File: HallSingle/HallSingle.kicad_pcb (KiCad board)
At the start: 2 copper layers, 12 x 23.5 mm, 12 parts, among them J1 Conn_01x03, U1 SS49E, U2 TS331ILT

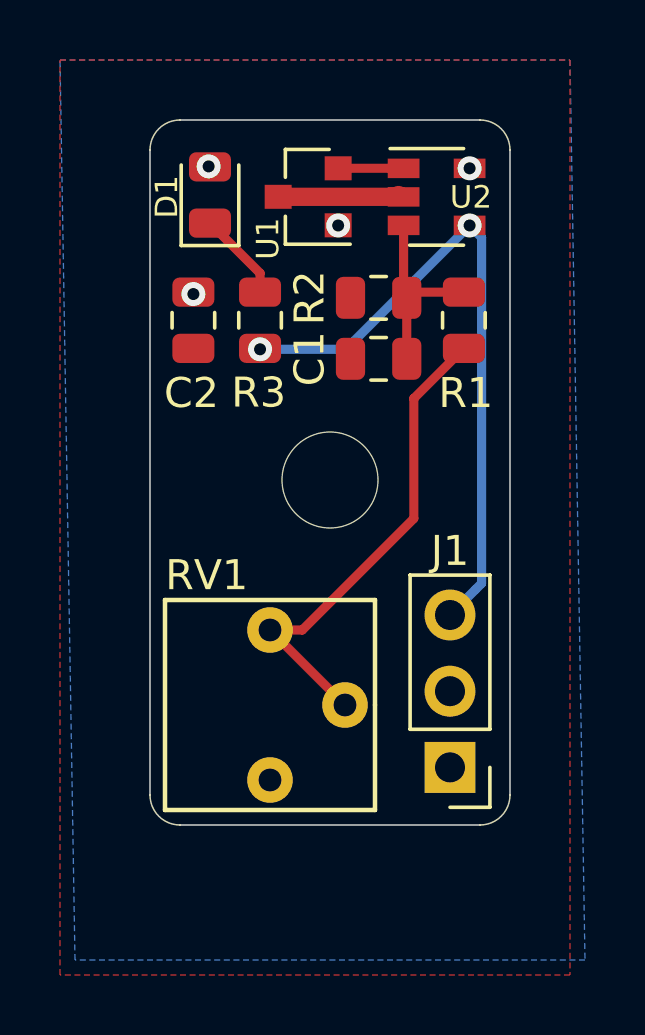
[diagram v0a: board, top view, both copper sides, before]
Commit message: Changed comparator to reverse - also NOTed  the led. this is to help with fault tolerance
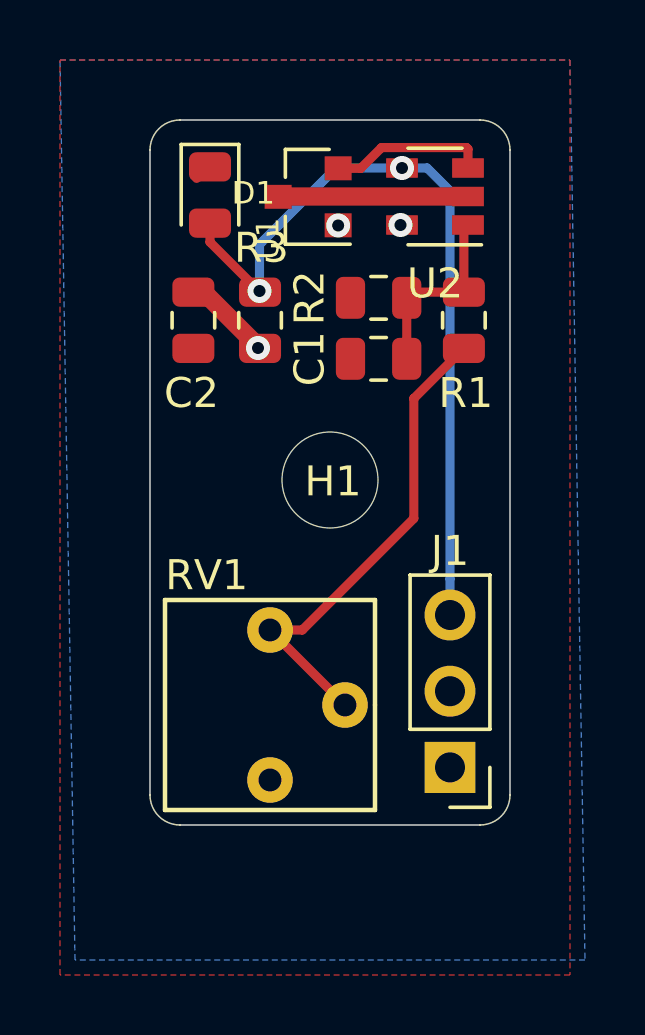
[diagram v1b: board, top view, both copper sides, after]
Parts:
- removed G***: LOGO, HallEffect:VoronLogo_6pt5mm_silkScreen
- removed REF**: MountingHole_3.2mm_M3, HallEffect:MountingHole_3.2mm_M3
- added H1: MountingHole, HallEffect:MountingHole_3.2mm_M3, F.Cu at (144.0, 69.0)
- U2: value TS331ILT -> TL331; footprint HallEffect:SOT-23-5 -> Package_TO_SOT_SMD:SOT-23-5
- moved U2 0.06 mm to (147.5, 59.5), turned to 180 degrees
- turned D1 to 270 degrees
- turned R3 to 90 degrees
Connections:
- D1 pad 1: Net-(D1-Pad1) -> GND
- D1 pad 2: +5V -> Signal
- R3 pad 1: Net-(D1-Pad1) -> +5V
- U2 pad 1: Net-(U1-Pad2) -> Net-(C1-Pad1)
- U2 pad 3: Net-(C1-Pad1) -> Net-(U1-Pad2)
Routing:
- net Signal: track 22.3 -> 26.5 mm
- net Net-(U1-Pad2): track 2.18 -> 5.27 mm
- net +5V: track 0.00 -> 3.00 mm, vias 4 -> 3
- net Net-(D1-Pad1): track 2.99 -> 0.00 mm
- net GND: track 4.27 -> 6.90 mm

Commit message: Resolved some design rule issues. update jpg
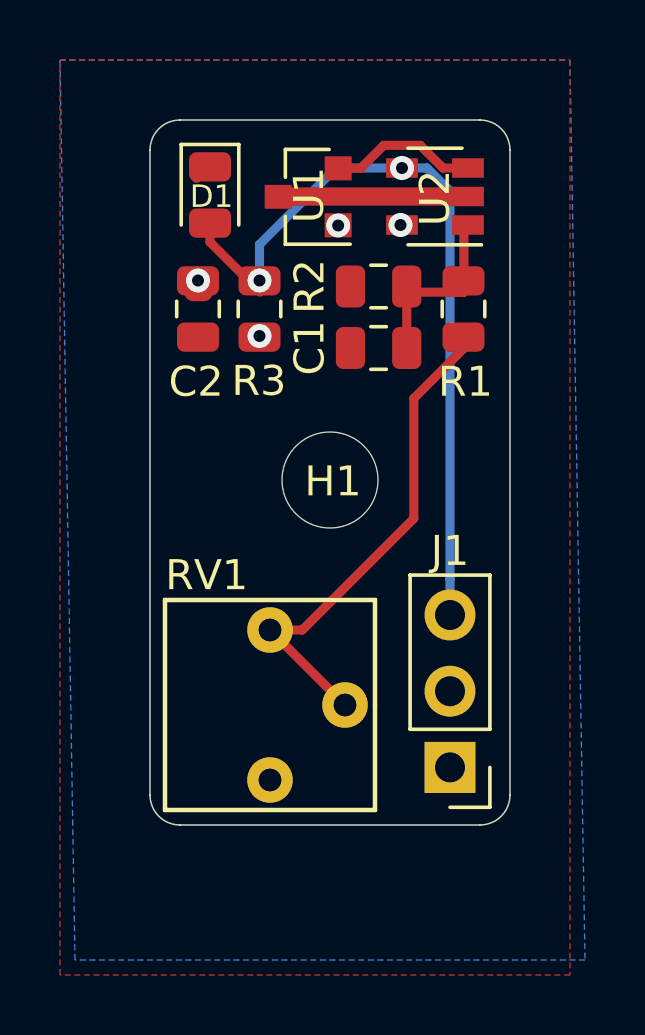
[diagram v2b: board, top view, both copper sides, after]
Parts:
- moved C2 0.41 mm to (139.6, 63.3)
- moved R2 0.38 mm to (145.6, 62.5)
- moved R3 0.38 mm to (141.7, 63.3)
- moved R1 0.38 mm to (148.4, 63.3)
- moved C1 0.36 mm to (145.6, 64.6)
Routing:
- net +5V: track 3.00 -> 0.35 mm, vias 3 -> 4
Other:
- board text added: "NC V1.0"

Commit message: Corrected wiring to comparator to NC config. Updated header to be same config as SKR - straight through cable required. update revision number
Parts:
- turned U2 to 0 degrees
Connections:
- J1 pad 1: +5V -> Signal
- J1 pad 3: Signal -> +5V
- U2 pad 1: Net-(C1-Pad1) -> Net-(U1-Pad2)
- U2 pad 3: Net-(U1-Pad2) -> Net-(C1-Pad1)
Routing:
- net +5V: track 0.35 -> 4.45 mm
- net Signal: track 26.5 -> 30.5 mm
- net Net-(U1-Pad2): track 4.96 -> 2.14 mm
- net GND: track 6.90 -> 4.70 mm
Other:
- board text added: "NC V1.1"
- board text removed: "NC V1.0"
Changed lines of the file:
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@@
     (thickness 1.6)
     (drawings 12)
-    (tracks 40)
+    (tracks 51)
     (zones 0)
     (modules 11)
@@
   )
   (module Package_TO_SOT_SMD:SOT-23-5 (layer F.Cu)
-    (at 147.5 59.55 180)
+    (at 147.5 59.55)
     (descr "5-pin SOT23 package")
     (tags SOT-23-5)
@@
       (effects (font (size 0.5 0.5) (thickness 0.075)))
     )
-    (pad 5 smd rect (at 1.1 -0.95 180) (size 1.06 0.65) (layers F.Cu F.Paste F.Mask)
+    (pad 5 smd rect (at 1.1 -0.95) (size 1.06 0.65) (layers F.Cu F.Paste F.Mask)
       (net 3 +5V))
-    (pad 4 smd rect (at 1.1 0.95 180) (size 1.06 0.65) (layers F.Cu F.Paste F.Mask)
+    (pad 4 smd rect (at 1.1 0.95) (size 1.06 0.65) (layers F.Cu F.Paste F.Mask)
       (net 4 Signal))
-    (pad 3 smd rect (at -1.1 0.95 180) (size 1.06 0.65) (layers F.Cu F.Paste F.Mask)
+    (pad 3 smd rect (at -1.1 0.95) (size 1.06 0.65) (layers F.Cu F.Paste F.Mask)
+      (net 2 "Net-(C1-Pad1)"))
+    (pad 2 smd rect (at -1.1 0) (size 1.06 0.65) (layers F.Cu F.Paste F.Mask)
+      (net 1 GND))
+    (pad 1 smd rect (at -1.1 -0.95) (size 1.06 0.65) (layers F.Cu F.Paste F.Mask)
       (net 6 "Net-(U1-Pad2)"))
-    (pad 2 smd rect (at -1.1 0 180) (size 1.06 0.65) (layers F.Cu F.Paste F.Mask)
-      (net 1 GND))
-    (pad 1 smd rect (at -1.1 -0.95 180) (size 1.06 0.65) (layers F.Cu F.Paste F.Mask)
-      (net 2 "Net-(C1-Pad1)"))
     (model ${KISYS3DMOD}/Package_TO_SOT_SMD.3dshapes/SOT-23-5.wrl
       (at (xyz 0 0 0))
@@
     (fp_line (start -0.635 -1.27) (end 1.27 -1.27) (layer F.Fab) (width 0.1))
     (pad 3 thru_hole oval (at 0 5.08 180) (size 1.7 1.7) (drill 1) (layers *.Cu *.Mask)
+      (net 3 +5V))
+    (pad 2 thru_hole oval (at 0 2.54 180) (size 1.7 1.7) (drill 1) (layers *.Cu *.Mask)
+      (net 1 GND))
+    (pad 1 thru_hole rect (at 0 0 180) (size 1.7 1.7) (drill 1) (layers *.Cu *.Mask)
       (net 4 Signal))
-    (pad 2 thru_hole oval (at 0 2.54 180) (size 1.7 1.7) (drill 1) (layers *.Cu *.Mask)
-      (net 1 GND))
-    (pad 1 thru_hole rect (at 0 0 180) (size 1.7 1.7) (drill 1) (layers *.Cu *.Mask)
-      (net 3 +5V))
     (model ${KIPRJMOD}/Library/3D_Packages/PinHeader_1x03_P2.54mm_Vertical.step
       (at (xyz 0 0 0))
@@
     )
   )
-  (gr_text "NC V1.0\n" (at 139.15 69.05 90) (layer B.SilkS)
+  (gr_text "NC V1.1\n" (at 139.15 69.05 90) (layer B.SilkS)
     (effects (font (size 1 1) (thickness 0.15)) (justify mirror))
   )
@@
   (gr_line (start 150 58) (end 150 79.5) (layer Edge.Cuts) (width 0.05))
   (gr_line (start 139 57) (end 149 57) (layer Edge.Cuts) (width 0.05))
+  (segment (start 139.554001 58.946999) (end 139.954 58.547) (width 0.3048) (layer F.Cu) (net 1))
   (segment (start 142.2825 59.55) (end 142.272 59.5605) (width 0.6096) (layer F.Cu) (net 1))
-  (segment (start 148.6 59.55) (end 142.2825 59.55) (width 0.6096) (layer F.Cu) (net 1))
-  (segment (start 139.554001 58.946999) (end 139.954 58.547) (width 0.3048) (layer F.Cu) (net 1))
+  (segment (start 146.4 59.55) (end 142.2825 59.55) (width 0.6096) (layer F.Cu) (net 1))
   (segment (start 148.45 62.725) (end 148.463 62.738) (width 0.3048) (layer F.Cu) (net 2))
   (segment (start 147.9885 62.738) (end 148.463 62.738) (width 0.3048) (layer F.Cu) (net 2))
   (segment (start 146.4535 62.824) (end 146.558 62.9285) (width 0.3048) (layer F.Cu) (net 2))
   (segment (start 146.7485 62.738) (end 146.558 62.9285) (width 0.3048) (layer F.Cu) (net 2))
-  (segment (start 148.463 62.738) (end 146.7485 62.738) (width 0.3048) (layer F.Cu) (net 2))
+  (segment (start 148.463 62.45) (end 146.7485 62.45) (width 0.3048) (layer F.Cu) (net 2))
   (segment (start 146.558 64.9605) (end 146.558 62.9285) (width 0.3048) (layer F.Cu) (net 2))
-  (segment (start 148.463 60.637) (end 148.6 60.5) (width 0.3048) (layer F.Cu) (net 2))
-  (segment (start 148.463 62.738) (end 148.463 60.637) (width 0.3048) (layer F.Cu) (net 2))
-  (via (at 141.65 64.2) (size 0.8) (drill 0.4) (layers F.Cu B.Cu) (net 3))
-  (via (at 146.35 60.5) (size 0.8) (drill 0.4) (layers F.Cu B.Cu) (net 3))
-  (via (at 144.272 60.5155) (size 0.8) (drill 0.4) (layers F.Cu B.Cu) (net 3))
+  (segment (start 146.4 62.392) (end 146.558 62.55) (width 0.3048) (layer F.Cu) (net 2))
+  (segment (start 146.4 60.5) (end 146.4 62.392) (width 0.3048) (layer F.Cu) (net 2))
+  (via (at 142.4 63.5) (size 0.8) (drill 0.4) (layers F.Cu B.Cu) (net 3))
+  (via (at 145.15 60.5) (size 0.8) (drill 0.4) (layers F.Cu B.Cu) (net 3))
   (segment (start 139.446 62.738) (end 139.446 62.738) (width 0.6096) (layer F.Cu) (net 3))
   (segment (start 139.446 62.738) (end 139.7935 62.738) (width 0.6096) (layer F.Cu) (net 3))
-  (via (at 139.6 62.35) (size 0.8) (drill 0.4) (layers F.Cu B.Cu) (net 3))
-  (via (at 146.4 58.6) (size 0.8) (drill 0.4) (layers F.Cu B.Cu) (net 4))
-  (via (at 141.65 62.35) (size 0.8) (drill 0.4) (layers F.Cu B.Cu) (net 4))
-  (segment (start 146.451 58.6105) (end 146.4535 58.613) (width 0.3048) (layer F.Cu) (net 4))
-  (segment (start 140 61.0695) (end 141.6685 62.738) (width 0.3048) (layer F.Cu) (net 4))
-  (segment (start 140 60.4375) (end 140 61.0695) (width 0.3048) (layer F.Cu) (net 4))
-  (segment (start 148 73.5) (end 148 73.6) (width 0.3048) (layer B.Cu) (net 4))
-  (segment (start 148 72.297919) (end 148 73.5) (width 0.3048) (layer B.Cu) (net 4))
-  (segment (start 147.2348 58.6) (end 148 59.3652) (width 0.3048) (layer B.Cu) (net 4))
-  (segment (start 148 59.3652) (end 148 72.297919) (width 0.3048) (layer B.Cu) (net 4))
-  (segment (start 146.4 58.6) (end 147.2348 58.6) (width 0.3048) (layer B.Cu) (net 4))
-  (segment (start 141.65 61.15) (end 141.65 62.7) (width 0.3048) (layer B.Cu) (net 4))
-  (segment (start 146.4 58.6) (end 144.2 58.6) (width 0.3048) (layer B.Cu) (net 4))
-  (segment (start 144.2 58.6) (end 141.65 61.15) (width 0.3048) (layer B.Cu) (net 4))
+  (via (at 139.05 61.45) (size 0.8) (drill 0.4) (layers F.Cu B.Cu) (net 3))
+  (via (at 148.9 59.4) (size 0.8) (drill 0.4) (layers F.Cu B.Cu) (net 3))
+  (segment (start 148.6 59.1) (end 148.9 59.4) (width 0.6096) (layer F.Cu) (net 3))
+  (segment (start 148.6 58.6) (end 148.6 59.1) (width 0.6096) (layer F.Cu) (net 3))
+  (segment (start 139.6 62) (end 139.05 61.45) (width 0.6096) (layer F.Cu) (net 3))
+  (segment (start 139.6 62.3625) (end 139.6 62) (width 0.6096) (layer F.Cu) (net 3))
+  (segment (start 145.1395 60.5105) (end 145.15 60.5) (width 0.6096) (layer F.Cu) (net 3))
+  (segment (start 144.272 60.5105) (end 145.1395 60.5105) (width 0.6096) (layer F.Cu) (net 3))
+  (segment (start 141.6625 64.2375) (end 142.4 63.5) (width 0.6096) (layer F.Cu) (net 3))
+  (segment (start 141.65 64.2375) (end 141.6625 64.2375) (width 0.6096) (layer F.Cu) (net 3))
+  (segment (start 148 73.5) (end 148 73.6) (width 0.3048) (layer B.Cu) (net 3))
+  (segment (start 148.463 60.637) (end 148.6 60.5) (width 0.3048) (layer F.Cu) (net 4))
+  (via (at 149 61.25) (size 0.8) (drill 0.4) (layers F.Cu B.Cu) (net 4))
+  (via (at 140.9 61.4) (size 0.8) (drill 0.4) (layers F.Cu B.Cu) (net 4))
+  (segment (start 141.65 62.15) (end 140.9 61.4) (width 0.3048) (layer F.Cu) (net 4))
+  (segment (start 141.65 62.3625) (end 141.65 62.15) (width 0.3048) (layer F.Cu) (net 4))
+  (segment (start 140 60.5) (end 140.9 61.4) (width 0.3048) (layer F.Cu) (net 4))
+  (segment (start 140 60.4375) (end 140 60.5) (width 0.3048) (layer F.Cu) (net 4))
+  (segment (start 148.6 60.85) (end 149 61.25) (width 0.3048) (layer F.Cu) (net 4))
+  (segment (start 148.6 60.5) (end 148.6 60.85) (width 0.3048) (layer F.Cu) (net 4))
+  (segment (start 148.85 61.4) (end 149 61.25) (width 0.3048) (layer B.Cu) (net 4))
+  (segment (start 149.399999 61.649999) (end 149 61.25) (width 0.3048) (layer B.Cu) (net 4))
+  (segment (start 148 77.82429) (end 149.399999 76.424291) (width 0.3048) (layer B.Cu) (net 4))
+  (segment (start 149.399999 76.424291) (end 149.399999 61.649999) (width 0.3048) (layer B.Cu) (net 4))
+  (segment (start 148 78.58) (end 148 77.82429) (width 0.3048) (layer B.Cu) (net 4))
+  (segment (start 140.9 61.4) (end 141.299999 61.799999) (width 0.3048) (layer B.Cu) (net 4))
+  (segment (start 148.450001 61.799999) (end 149 61.25) (width 0.3048) (layer B.Cu) (net 4))
+  (segment (start 141.299999 61.799999) (end 148.450001 61.799999) (width 0.3048) (layer B.Cu) (net 4))
   (segment (start 143.07763 74) (end 142 74) (width 0.3048) (layer F.Cu) (net 5))
   (segment (start 148.463 64.613) (end 146.794399 66.281601) (width 0.3048) (layer F.Cu) (net 5))
@@
   (segment (start 146.794399 70.283231) (end 143.07763 74) (width 0.3048) (layer F.Cu) (net 5))
   (segment (start 144.5 76.5) (end 142 74) (width 0.3048) (layer F.Cu) (net 5))
-  (segment (start 147.7652 58.6) (end 147.009599 57.844399) (width 0.3048) (layer F.Cu) (net 6))
-  (segment (start 148.6 58.6) (end 147.7652 58.6) (width 0.3048) (layer F.Cu) (net 6))
-  (segment (start 145.0268 58.6105) (end 145.792901 57.844399) (width 0.3048) (layer F.Cu) (net 6))
-  (segment (start 145.792901 57.844399) (end 147.009599 57.844399) (width 0.3048) (layer F.Cu) (net 6))
-  (segment (start 144.272 58.6105) (end 145.0268 58.6105) (width 0.3048) (layer F.Cu) (net 6))
+  (segment (start 146.451 58.6105) (end 146.4535 58.608) (width 0.3048) (layer F.Cu) (net 6))
+  (segment (start 144.2825 58.6) (end 144.272 58.6105) (width 0.3048) (layer F.Cu) (net 6))
+  (segment (start 146.4 58.6) (end 144.2825 58.6) (width 0.3048) (layer F.Cu) (net 6))
   (zone (net 3) (net_name +5V) (layer B.Cu) (hatch edge 0.508)
     (connect_pads (clearance 0.508))
